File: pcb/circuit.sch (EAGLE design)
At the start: 136 parts, among them IC1 MCP73833-AMI/UN-ND, IC2 MCP3423, IC3 MCP1612-ADJI/MS, IC4 ATSAML22N18A, IC5 ATWINC1510-MR210PB1952-ND, IC6 RN4870, IC7 WE-TVS, J1 USB2-MICRO, J10 2.5MM-AUDIO-JACK-MONO, J11 2.5MM-AUDIO-JACK-MONO, J12 2.5MM-AUDIO-JACK-MONO, J13 2.5MM-AUDIO-JACK-MONO, J14 2.5MM-AUDIO-JACK-MONO, J2 S3B-XH-A, J3 2.5MM-AUDIO-JACK-MONO, J4 2.5MM-AUDIO-JACK-MONO, J5 2.5MM-AUDIO-JACK-MONO, J6 2.5MM-AUDIO-JACK-MONO, J7 2.5MM-AUDIO-JACK-MONO, J8 2.5MM-AUDIO-JACK-MONO, J9 2.5MM-AUDIO-JACK-MONO, Q1 32kHz, T1 PMOS, T10 NMOSSOT323, T11 NMOSSOT323, T12 NMOSSOT323, T13 NMOSSOT323, T2 NMOSSOT323, T3 NMOSSOT323, T4 NMOSSOT323, T5 NMOSSOT323, T6 NMOSSOT323, T7 NMOSSOT323, T8 NMOSSOT323, T9 NMOSSOT323, X1 B3S-1000

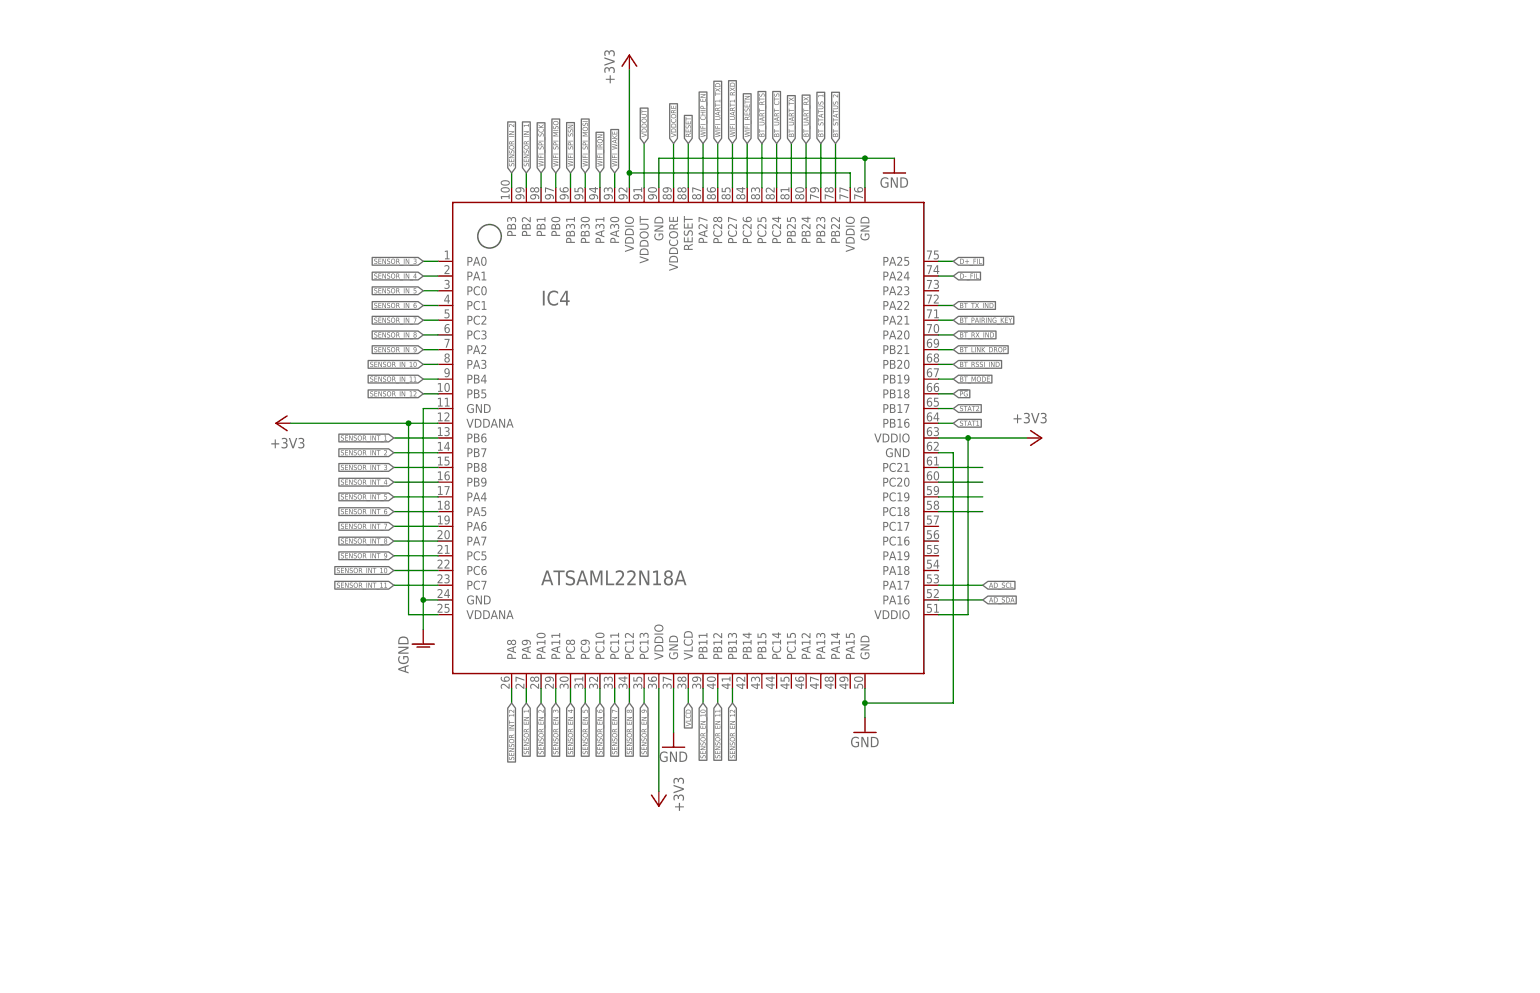
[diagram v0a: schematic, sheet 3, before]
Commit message: Schematic: - OLED added Datasheets: - SAML22 AppNotes added
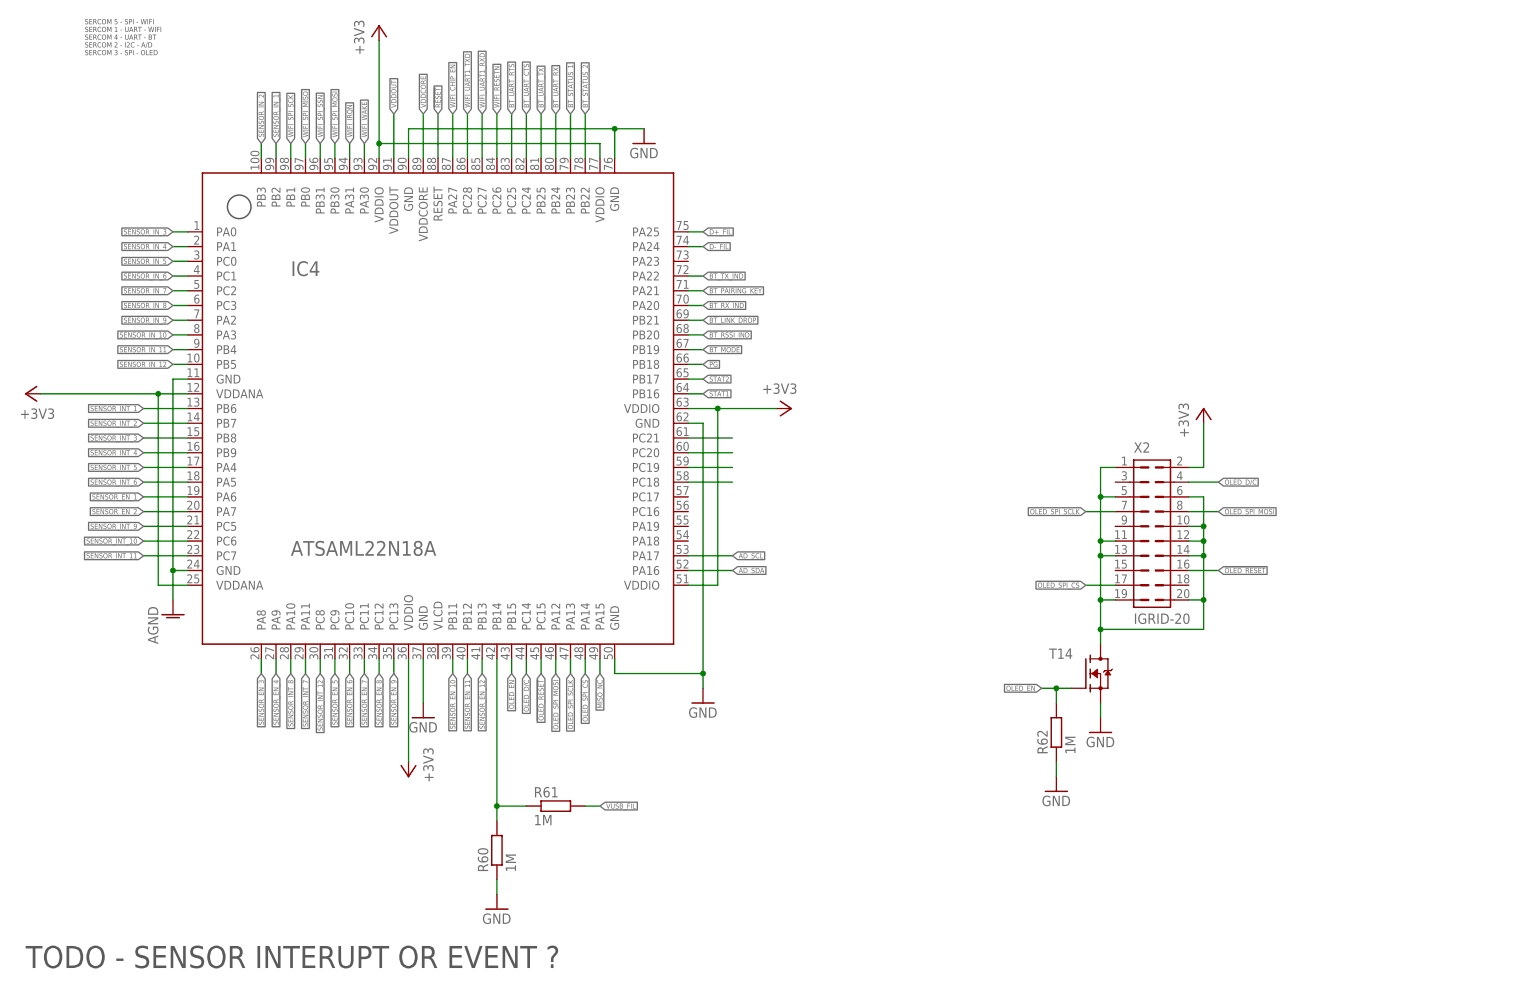
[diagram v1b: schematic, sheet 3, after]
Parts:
- added R60, R61, R62: 1M, rcl:R-EU_R0603
- added T14: NMOSSOT323, thermo:NMOSSOT323
- added X2: IGRID-20, thermo:IGRID-20
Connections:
- removed net VLCD: IC4.VLCD
- new net !OLED_RESET: IC4.PC15, X2.16
- new net !OLED_SPI_CS: IC4.PA14, X2.17
- new net MISO_NC: IC4.PA15
- new net N$31: IC4.PB14, R60.2, R61.1
- new net N$32: T14.D, X2.1, X2.10, X2.11, X2.12, X2.13, X2.14, X2.19, X2.20, X2.5, X2.6
- new net OLED_D/C: IC4.PC14, X2.4
- new net OLED_EN: IC4.PB15, R62.2, T14.G
- new net OLED_SPI_MOSI: IC4.PA12, X2.8
- new net OLED_SPI_SCLK: IC4.PA13, X2.7
- net +3V3: now also X2.2
- net GND: now also R60.1, R62.1, T14.S
- net SENSOR_EN_1: now also IC4.PA6; no longer IC4.PA9
- net SENSOR_EN_2: now also IC4.PA7; no longer IC4.PA10
- net SENSOR_EN_3: now also IC4.PA8; no longer IC4.PA11
- net SENSOR_EN_4: now also IC4.PA9; no longer IC4.PC8
- net SENSOR_INT_12: now also IC4.PC8; no longer IC4.PA8
- net SENSOR_INT_7: now also IC4.PA11; no longer IC4.PA6
- net SENSOR_INT_8: now also IC4.PA10; no longer IC4.PA7
- net VUSB_FIL: now also R61.2
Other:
- note added: "SERCOM 5 - SPI - WIFI SERCOM 1 - UART - WIFI SERCOM 4 - UART - BT SERCOM 2 - I2C - A/D SERCOM 3 - SPI - OLED"
- note added: "TODO - SENSOR INTERUPT OR EVENT ?"
- moved on the sheet: IC4

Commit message: Schematic
-added part numbers
-all devices are connected
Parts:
- removed J13, J14: 2.5MM-AUDIO-JACK-MONO, Thermo_Library:2.5MM-AUDIO-JACK-MONO
- removed R59: 4,7k, rcl:R-EU_R0603
- removed R60, R61, R62: 1M, rcl:R-EU_R0603
- removed T14: NMOSSOT323, thermo:NMOSSOT323
- added C27: 1nF, rcl:C-EUC0603
- added C33, C35, C36: 1µF, rcl:C-EUC0603
- added C34, C37: 100nF, rcl:C-EUC0603
- added IC8: ATSAML22N18A, Thermo_Library:ATSAML22N18A
- added JP1, JP2, JP4, JP7: (no value), jumper:JP4E
- added JP3: (no value), jumper:JP2E
- added JP5, JP6: (no value), jumper:JP1E
- added X3: MOLEX_1MM_FPC, thermo:MOLEX_1MM_FPC
- added X4: IGRID-20, thermo:IGRID-20
- C1, C2, C30, C5: OC_FARNELL 1735530 -> (none); OC_MOUSER (none) -> 81-GRM21BR61E106KA3L
- C10: value 100nF -> 1nF; device rcl:C-EUC0402 -> rcl:C-EUC0603; OC_FARNELL 2218856 -> (none); OC_MOUSER (none) -> 80-C0603C102K3R
- C11: value 100nF -> 4,7nF; device rcl:C-EUC0402 -> rcl:C-EUC0603; OC_FARNELL 2218856 -> (none); OC_MOUSER (none) -> 80-C0603C472K3R
- C12, C13, C14, C15, C19, C20, C3, C32, C6, C9: device rcl:C-EUC0402 -> rcl:C-EUC0603; OC_FARNELL 2218856 -> (none); OC_MOUSER (none) -> 581-06033C104KAT2A
- C16: value 1µF -> 100nF; device rcl:C-EUC0402 -> rcl:C-EUC0603; OC_FARNELL 2218856 -> (none); OC_MOUSER (none) -> 581-06033C104KAT2A
- C17, C18: value 22pF -> 10µF; device rcl:C-EUC0402 -> rcl:C-EUC0805; OC_FARNELL 2332500 -> (none); OC_MOUSER (none) -> 81-GRM21BR61E106KA3L
- C21, C22: value 10µF -> 100nF; device rcl:C-EUC0805 -> rcl:C-EUC0603; OC_FARNELL 1735530 -> (none); OC_MOUSER (none) -> 581-06033C104KAT2A
- C23: value 100nF -> 1µF; device rcl:C-EUC0402 -> rcl:C-EUC0603; OC_FARNELL 2218856 -> (none); OC_MOUSER (none) -> 810-CGA3E1X7R1E105AC
- C24: value 1µF -> 22pF; OC_FARNELL 2211179 -> (none); OC_MOUSER (none) -> 581-02013A220FAT2A
- C25: value 10µF -> 22pF; device rcl:C-EUC0805 -> rcl:C-EUC0603; OC_FARNELL 1735530 -> (none); OC_MOUSER (none) -> 581-02013A220FAT2A
- C26: value 10nF -> 10µF; device rcl:C-EUC0402 -> rcl:C-EUC0805; OC_FARNELL 1828887 -> (none); OC_MOUSER (none) -> 81-GRM21BR61E106KA3L
- C28: value 10nF -> 100nF; device rcl:C-EUC0402 -> rcl:C-EUC0603; OC_FARNELL 1828887 -> (none); OC_MOUSER (none) -> 581-06033C104KAT2A
- C29: value 4,7nF -> 10µF; device rcl:C-EUC0603 -> rcl:C-EUC0805; OC_FARNELL 1759098 -> (none); OC_MOUSER (none) -> 81-GRM21BR61E106KA3L
- C31: value 10µF -> 1nF; device rcl:C-EUC0805 -> rcl:C-EUC0603; OC_FARNELL 1735530 -> (none); OC_MOUSER (none) -> 80-C0603C102K3R
- C4, C7: device rcl:C-EUC0402 -> rcl:C-EUC0603; OC_FARNELL 1758911 -> (none); OC_MOUSER (none) -> 80-C0603C102K3R
- C8: value 100nF -> 10µF; device rcl:C-EUC0402 -> rcl:C-EUC0805; OC_FARNELL 2218856 -> (none); OC_MOUSER (none) -> 81-GRM21BR61E106KA3L
- D1: value BAT60AE6327HTSA1 -> Red; device Thermo_Library:BAT60AE6327HTSA1 -> Thermo_Library:LED-2012; OC_FARNELL 2432679 -> (none); OC_MOUSER (none) -> 630-HSMC-C170-T0000
- D2: value Red -> Green; OC_FARNELL 2750579 -> (none); OC_MOUSER (none) -> 630-HSMQ-C170-T0000
- D3: value Green -> Blue; OC_FARNELL 2750574 -> (none); OC_MOUSER (none) -> 630-HSMR-C170-R0000
- D4: value Blue -> BAT60AE6327HTSA1; device Thermo_Library:LED-2012 -> Thermo_Library:BAT60AE6327HTSA1; OC_FARNELL 2750580 -> (none); OC_MOUSER (none) -> 726-BAT60AE6327HTSA1
- IC1: OC_MOUSER (none) -> 579-MCP73833T-AMI/UN
- IC2: device Thermo_Library:MCP3423 -> thermo:MCP3423; OC_MOUSER (none) -> 579-MCP3423-E/UN
- IC3: device Thermo_Library:MCP1612-ADJI/MS -> thermo:MCP1612-ADJI/MS; OC_MOUSER (none) -> 579-MCP1612T-ADJI/MS
- IC4: value ATSAML22N18A -> WE-TVS; device Thermo_Library:ATSAML22N18A -> thermo:WE-TVS; OC_MOUSER (none) -> 710-824011
- IC5: OC_MOUSER (none) -> 556-1510MR210UB1140
- IC6: OC_MOUSER (none) -> 579-RN4870-V/RM118
- IC7: value WE-TVS -> MAX3378EEUD; device Thermo_Library:WE-TVS -> thermo:MAX3378EEUD; OC_MOUSER (none) -> 700-MAX3378EEUD
- J1: device Thermo_Library:USB2-MICRO -> thermo:USB2-MICRO; OC_MOUSER (none) -> 649-10104110-0001LF
- J10, J11, J3, J4, J5, J6, J7, J8, J9: OC_MOUSER (none) -> 490-MJ-2523-SMT-TR
- J12: value 2.5MM-AUDIO-JACK-MONO -> 22-05-7028-02; device Thermo_Library:2.5MM-AUDIO-JACK-MONO -> con-molex:22-05-7028-02; OC_MOUSER (none) -> 538-22-05-7028
- J2: value S3B-XH-A -> 2.5MM-AUDIO-JACK-MONO; device Thermo_Library:S3B-XH-A -> Thermo_Library:2.5MM-AUDIO-JACK-MONO; OC_FARNELL 2401852 -> (none); OC_MOUSER (none) -> 490-MJ-2523-SMT-TR
- L1: OC_FARNELL 2467201 -> (none); OC_MOUSER (none) -> 710-74437321033
- L2: value 10µH -> L-0603; device Thermo_Library:L-1210 -> Thermo_Library:L-0603; OC_FARNELL 1299975 -> (none); OC_MOUSER (none) -> 710-742792641
- L3: value L-0603 -> WE-CNSW; device Thermo_Library:L-0603 -> thermo:WE-CNSW; OC_FARNELL 1635705 -> (none); OC_MOUSER (none) -> 710-744232090
- L4: value WE-CNSW -> 10µH; device Thermo_Library:WE-CNSW -> Thermo_Library:L-1210; OC_MOUSER (none) -> 871-B82422H1103K
- L5: OC_FARNELL 1515716 -> (none); OC_MOUSER (none) -> 81-BLM18EG221SN1D
- R1: value 1M -> 270; OC_FARNELL 2447285 -> (none); OC_MOUSER (none) -> 652-CR0603FX-2700ELF
- R10: value 1.8M -> 2.2M; OC_FARNELL 9238875 -> (none); OC_MOUSER (none) -> 603-RC0603FR-072M2L
- R11: value 301k -> 1.8M; device rcl:R-EU_R0402 -> rcl:R-EU_R0603; OC_FARNELL 2059188 -> (none); OC_MOUSER (none) -> 603-RC0603FR-071M8L
- R12: value 10 -> 301k; device rcl:R-EU_R0402 -> rcl:R-EU_R0603; OC_FARNELL 2059188 -> (none); OC_MOUSER (none) -> 603-RC0603FR-07301KL
- R13: value 324k -> 1M; device rcl:R-EU_R0402 -> rcl:R-EU_R0603; OC_FARNELL 2302893 -> (none); OC_MOUSER (none) -> 603-RC0603FR-071ML
- R14: value 25k -> 10; device rcl:R-EU_R0805 -> rcl:R-EU_R0603; OC_DIGIKEY A124124CT-ND -> (none); OC_MOUSER (none) -> 603-RC0603FR-0710RL
- R15: value 200k -> 324k; device rcl:R-EU_R0402 -> rcl:R-EU_R0603; OC_FARNELL 2059185 -> (none); OC_MOUSER (none) -> 603-RC0603FR-07324KL
- R16: value 10k -> 25k; device rcl:R-EU_R0603 -> rcl:R-EU_R0805; OC_MOUSER (none) -> 279-CPF0805B25KE1
- R17: value 330 -> 200k; OC_MOUSER (none) -> 603-RC0603FR-07200KL
- R18, R21, R22, R23, R24, R25, R29: OC_FARNELL 2447743 -> (none); OC_MOUSER (none) -> 603-RC0603JR-070RL
- R19, R26: value 0 -> 1M; OC_FARNELL 2447743 -> (none); OC_MOUSER (none) -> 603-RC0603FR-071ML
- R2: value 270 -> 4,7k; device rcl:R-EU_R0402 -> rcl:R-EU_R0603; OC_FARNELL 2447144 -> (none); OC_MOUSER (none) -> 603-RC0603FR-074K7L
- R20: value 0 -> 100k; OC_FARNELL 2447743 -> (none); OC_MOUSER (none) -> 603-RT0603FRE13100KL
- R27: value 4.7k -> 0; device rcl:R-EU_R0402 -> rcl:R-EU_R0603; OC_FARNELL 9239316 -> (none); OC_MOUSER (none) -> 603-RC0603JR-070RL
- R28: value 1M -> 0; OC_MOUSER (none) -> 603-RC0603JR-070RL
- R3: value 270 -> 4,7k; device rcl:R-EU_R0402 -> rcl:R-EU_R0603; OC_FARNELL 2447144 -> (none)
- R30: value 1M -> 0; OC_FARNELL 2447285 -> (none); OC_MOUSER (none) -> 603-RC0603JR-070RL
- R31, R34, R48, R49, R50, R55, R56, R57: OC_FARNELL 2447285 -> (none); OC_MOUSER (none) -> 603-RC0603FR-071ML
- R32: value 1M -> 4,7k; OC_FARNELL 2447285 -> (none)
- R33: value 4,8k -> 0; OC_FARNELL 2447442 -> (none); OC_MOUSER (none) -> 603-RC0603JR-070RL
- R35, R51, R52, R53, R54: value 4,8k -> 1M; OC_FARNELL 2447442 -> (none); OC_MOUSER (none) -> 603-RC0603FR-071ML
- R36: value 4,8k -> 10k; OC_FARNELL 2447442 -> (none); OC_MOUSER (none) -> 603-RC0603FR-0710KL
- R37: value 1M -> 330; OC_FARNELL 2447285 -> (none); OC_MOUSER (none) -> 603-RC0603FR-07330RL
- R38, R43, R44, R45, R46: value 4,8k -> 4.7k 0.1%; OC_FARNELL 2447442 -> (none); OC_MOUSER (none) -> 279-CPF0603B4K7E1
- R39, R40, R41, R42, R47: value 1M -> 4.7k 0.1%; OC_FARNELL 2447285 -> (none); OC_MOUSER (none) -> 279-CPF0603B4K7E1
- R4: value 1.54k -> 100m; device rcl:R-EU_R0805 -> rcl:R-EU_R5025; OC_FARNELL 2670154 -> (none); OC_MOUSER (none) -> 652-CRM2010FXR100ELF
- R5: device rcl:R-EU_R0402 -> rcl:R-EU_R0603
- R58: value 4,7k -> 1M; OC_MOUSER (none) -> 603-RC0603FR-071ML
- R6: value 2k -> 1.54k; device rcl:R-EU_R0805 -> rcl:R-EU_R0603; OC_FARNELL 2447622 -> (none); OC_MOUSER (none) -> 660-RK73H1JTTD1541F
- R7: value 69.8k -> 270; device rcl:R-EU_R0805 -> rcl:R-EU_R0603; OC_FARNELL 1141002 -> 2447144
- R8: value 100m -> 2k; device rcl:R-EU_R5025 -> rcl:R-EU_R0603; OC_MOUSER (none) -> 652-CR0603-FX-2001LF
- R9: value 2.2M -> 69.8k; OC_FARNELL 2078930 -> (none); OC_MOUSER (none) -> 754-RR1220P-6982D-M
- SV1: value (none) -> JTAGEDU; OC_FARNELL 1392410 -> (none); OC_MOUSER (none) -> 538-70246-2004
- T1: device Thermo_Library:PMOS -> thermo:PMOS; OC_MOUSER (none) -> 781-SI2301CDS-T1-GE3
- T10, T11, T12, T13, T3, T4, T5, T6, T7, T8, T9: OC_FARNELL 2617470 -> (none); OC_MOUSER (none) -> 726-SP000917562
- T2: value NMOSSOT323 -> PMOS; device Thermo_Library:NMOSSOT323 -> thermo:PMOS; OC_FARNELL 2617470 -> (none); OC_MOUSER (none) -> 781-SI2301CDS-T1-GE3
- X1: value B3S-1000 -> LI-ION_BATHOL2; device Thermo_Library:B3S-1000 -> thermo:LI-ION_BATHOL2; OC_MOUSER (none) -> 534-1048
- X2: value IGRID-20 -> B3S-1000; device thermo:IGRID-20 -> Thermo_Library:B3S-1000; OC_MOUSER (none) -> 653-B3S-1000
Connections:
- removed net BAT_IN: IC2.CH1+, J2.VBAT+, R8.1, R9.1
- removed net N$10: C7.2, R14.2
- removed net N$11: C6.1, IC3.VCC, R12.1
- removed net N$18: R51.2, T13.D
- removed net N$25: IC4.PC21
- removed net N$26: IC4.PC20
- removed net N$27: IC4.PC19
- removed net N$28: IC4.PC18
- removed net N$31: IC4.PB14, R60.2, R61.1
- removed net N$9: IC3.COMP, R14.1
- removed net SENSOR_EN_10: IC4.PB11, R55.2
- removed net SENSOR_EN_11: IC4.PB12, R56.2
- removed net SENSOR_EN_12: IC4.PB13, R57.2
- removed net SENSOR_INT_10: IC4.PC6, J12.3
- removed net SENSOR_INT_11: IC4.PC7, J13.3
- removed net SENSOR_INT_12: IC4.PC8, J14.3
- removed net SENSOR_IN_10: IC4.PA3, J12.1, R53.1
- removed net SENSOR_IN_11: IC4.PB4, J13.1, R52.1
- removed net SENSOR_IN_12: IC4.PB5, J14.1, R51.1
- new net !PG!_TRANS: IC7.I/OVL1, IC8.PB18
- new net BUCK_RC_C: C10.2, R16.2
- new net BUCK_RC_R: IC3.COMP, R16.1
- new net BUCK_VCC: C9.1, IC3.VCC, R14.1
- new net EXT_PWM_0: IC8.PA19, J12-1.S
- new net EXT_PWM_1: IC8.PA18, J12-2.S
- new net RES0: IC8.PB13, JP3.1
- new net RES1: IC8.PB12, JP3.2
- new net RES2: IC8.PB11, JP3.3
- new net SENSOR_EN_0: IC8.PA4, R48.2, T3.G
- new net SENSOR_INT_0: IC8.PC8, J2.3
- new net SENSOR_IN_0: IC8.PB2, J2.1, R38.1
- new net SOF_NC: IC8.PA23
- new net STAT1_TRANS: IC7.I/OVL3, IC8.PB17
- new net STAT2_TRANS: IC7.I/OVL2, IC8.PB16
- new net UI_BUTTON_INT_0: IC8.PC21, X3.2
- new net UI_BUTTON_INT_1: IC8.PC20, X3.3
- new net UI_BUTTON_INT_2: IC8.PC19, X3.4
- new net UI_BUTTON_INT_3: IC8.PC18, X3.5
- new net USB_CON_INT_TRANS: IC7.I/OVL4, IC8.PB14
- new net VBAT_MEAS: C1.1, IC1.VBAT@1, IC1.VBAT@2, IC2.CH1-, R4.2, T1.D
- new net VIN: JP7.2, T2.D, X1.VBAT+
- net !OLED_RESET: now also IC8.PC15, X4.16; no longer IC4.PC15, X2.16
- net !OLED_SPI_CS: now also IC8.PA14, JP2.3, X4.17; no longer IC4.PA14, X2.17
- net !PG!: now also IC7.I/OVCC1, R7.2; no longer IC4.PB18, R5.2
- net !RESET!: now also C37.1, IC8.RESET, R36.1, R37.2; no longer C20.1, IC4.RESET, R16.1, R17.2
- net +3V3: now also C13.1, C14.1, C15.1, C16.1, C17.1, C2.1, C26.1, C27.1, C29.1, C34.1, C35.1, C6.1, C7.1, IC7.VL, IC8.VDDANA@1, IC8.VDDANA@2, IC8.VDDIO@1, IC8.VDDIO@2, IC8.VDDIO@3, IC8.VDDIO@4, IC8.VDDIO@5, J2.2, JP7.1, R12.2, R2.2, R26.2, R3.2, R32.2, R36.2, X3.1, X4.2; no longer C1.1, C10.1, C11.1, C21.1, C23.1, C25.1, C32.1, C8.1, IC4.VDDANA@1, IC4.VDDANA@2, IC4.VDDIO@1, IC4.VDDIO@2, IC4.VDDIO@3, IC4.VDDIO@4, IC4.VDDIO@5, J12.2, J13.2, J14.2, R11.2, R16.2, R27.2, R28.2, R58.2, R59.2, X2.2
- net AD_SCL: now also IC8.PA17, JP5.1, R2.1; no longer IC4.PA17, R58.1
- net AD_SDA: now also IC8.PA16, JP5.2, R3.1; no longer IC4.PA16, R59.1
- net AGND: now also C10.1, C11.2, C18.2, C19.2, C20.2, C21.2, IC8.GND@1, IC8.GND@2, R17.1, R18.2, R19.1; no longer C14.2, C15.2, C22.2, C29.2, C6.2, C7.1, IC4.GND@1, IC4.GND@2, R15.1, R32.1, T13.S, T2.S
- net BT_LINK_DROP: now also IC8.PB21; no longer IC4.PB21
- net BT_MODE: now also IC8.PB19, R31.1; no longer IC4.PB19, R28.1
- net BT_PAIRING_KEY: now also IC8.PA21; no longer IC4.PA21
- net BT_RSSI_IND: now also IC8.PB20; no longer IC4.PB20
- net BT_RX_IND: now also IC8.PA20; no longer IC4.PA20
- net BT_STATUS_1: now also IC8.PB23; no longer IC4.PB23
- net BT_STATUS_2: now also IC8.PB22; no longer IC4.PB22
- net BT_TX_IND: now also IC8.PA22; no longer IC4.PA22
- net BT_UART_CTS: now also IC8.PC24, JP4.2; no longer IC4.PC24
- net BT_UART_RTS: now also IC8.PC25, JP4.1; no longer IC4.PC25
- net BT_UART_RX: now also IC8.PB24, JP4.4; no longer IC4.PB24
- net BT_UART_TX: now also IC8.PB25, JP4.3; no longer IC4.PB25
- net D+: now also IC4.D+, L3.1; no longer IC7.D+, L4.1
- net D+_FIL: now also IC8.PA25, L3.2; no longer IC4.PA25, L4.2
- net D-: now also IC4.D-, L3.4; no longer IC7.D-, L4.4
- net D-_FIL: now also IC8.PA24, L3.3; no longer IC4.PA24, L4.3
- net FB: now also R15.1, R17.2; no longer R13.1, R15.2
- net GND: now also C14.2, C15.2, C22.2, C27.2, C29.2, C33.2, C34.2, C35.2, C36.2, C37.2, C6.2, C7.2, IC4.GND, IC8.GND@3, IC8.GND@4, IC8.GND@5, IC8.GND@6, IC8.GND@7, JP7.3, JP7.4, R11.1, R13.1, R18.1, R20.1, R35.1, R51.1, R52.1, R53.1, R54.1, R58.1, R8.1, R9.1, T13.S, X1.VBAT-, X2.P, X3.6; no longer C10.2, C11.2, C18.2, C19.2, C20.2, C21.2, IC4.GND@3, IC4.GND@4, IC4.GND@5, IC4.GND@6, IC4.GND@7, J2.VBAT-, R1.1, R10.1, R30.1, R37.1, R39.1, R40.1, R41.1, R42.1, R47.1, R6.1, R60.1, R62.1, R7.1, T14.S, X1.P
- net MISO_NC: now also IC8.PA15, JP2.4; no longer IC4.PA15
- net N$1: now also R11.2; no longer R9.2
- net N$12: now also D1.C, R1.1; no longer D2.C, R2.1
- net N$13: now also R12.1, R15.2; no longer R11.1, R13.2
- net N$14: now also D2.C, R5.1; no longer D3.C, R3.1
- net N$15: now also D3.C, R7.1; no longer D4.C, R5.1
- net N$16: now also R47.2, T12.D; no longer R53.2, T10.D
- net N$17: now also R20.2, T2.G; no longer R52.2, T12.D
- net N$2: now also R39.2, T4.D; no longer R46.2, T7.D
- net N$20: now also R40.2, T5.D; no longer R36.2, T2.D
- net N$21: now also R42.2, T7.D; no longer R35.2, T4.D
- net N$22: now also R44.2, T9.D; no longer R33.2, T5.D
- net N$23: now also C18.1, C19.1, C20.1; no longer C14.1, C22.1, C9.1
- net N$24: now also R21.2; no longer R29.2
- net N$29: now also R27.2; no longer R22.2
- net N$3: now also R41.2; no longer R45.2
- net N$30: now also R25.2; no longer R21.2
- net N$32: now also T13.D, X4.1, X4.10, X4.11, X4.12, X4.13, X4.14, X4.19, X4.20, X4.5, X4.6; no longer T14.D, X2.1, X2.10, X2.11, X2.12, X2.13, X2.14, X2.19, X2.20, X2.5, X2.6
- net N$37: now also C11.1, R19.2; no longer C29.1, R32.2
- net N$4: now also R43.2; no longer R44.2
- net N$45: now also R26.1; no longer R31.1
- net N$48: now also C30.1, C32.1; no longer C13.1, C26.1
- net N$5: now also R45.2, T10.D; no longer R43.2, T9.D
- net N$57: now also C33.1, R32.1; no longer C24.1, R27.1
- net N$6: now also R46.2; no longer R54.2
- net N$7: now also R37.1, X2.S; no longer R17.1, X1.S
- net NTC: now also R6.1, R9.2; no longer J2.NTC, R4.1, R7.2
- net OLED_D/C: now also IC8.PC14, X4.4; no longer IC4.PC14, X2.4
- net OLED_EN: now also IC8.PB15, R58.2, T13.G; no longer IC4.PB15, R62.2, T14.G
- net OLED_SPI_MOSI: now also IC8.PA12, JP2.1, X4.8; no longer IC4.PA12, X2.8
- net OLED_SPI_SCLK: now also IC8.PA13, JP2.2, X4.7; no longer IC4.PA13, X2.7
- net PROG: now also R8.2; no longer R6.2
- net RESET: now also C22.1; no longer C19.1
- net SENSOR_EN_1: now also IC8.PA5, R49.2, T5.G; no longer IC4.PA6, R37.2, T3.G
- net SENSOR_EN_2: now also IC8.PA6, R50.2, T7.G; no longer IC4.PA7, R39.2, T2.G
- net SENSOR_EN_3: now also IC8.PA7, R51.2, T9.G; no longer IC4.PA8, R40.2, T4.G
- net SENSOR_EN_4: now also IC8.PC5, R52.2, T11.G; no longer IC4.PA9, R41.2, T5.G
- net SENSOR_EN_5: now also IC8.PC6, R53.2, T4.G; no longer IC4.PC9, R42.2, T7.G
- net SENSOR_EN_6: now also IC8.PC7, R54.2; no longer IC4.PC10, R47.2
- net SENSOR_EN_7: now also IC8.PA9, R55.2; no longer IC4.PC11, R48.2
- net SENSOR_EN_8: now also IC8.PA10, R56.2, T10.G; no longer IC4.PC12, R49.2, T9.G
- net SENSOR_EN_9: now also IC8.PA11, R57.2, T12.G; no longer IC4.PC13, R50.2
- net SENSOR_INT_1: now also IC8.PC9, J4.3; no longer IC4.PB6, J3.3
- net SENSOR_INT_2: now also IC8.PC10, J6.3; no longer IC4.PB7, J4.3
- net SENSOR_INT_3: now also IC8.PC11, J8.3; no longer IC4.PB8, J5.3
- net SENSOR_INT_4: now also IC8.PC12, J10.3; no longer IC4.PB9, J6.3
- net SENSOR_INT_5: now also IC8.PC13, J3.3; no longer IC4.PA4, J7.3
- net SENSOR_INT_6: now also IC8.PB6, J5.3; no longer IC4.PA5, J8.3
- net SENSOR_INT_7: now also IC8.PB7, J7.3; no longer IC4.PA11, J9.3
- net SENSOR_INT_8: now also IC8.PB8, J9.3; no longer IC4.PA10, J10.3
- net SENSOR_INT_9: now also IC8.PB9; no longer IC4.PC5
- net SENSOR_IN_1: now also IC8.PB3, J4.1, R40.1; no longer IC4.PB2, J3.1, R38.1
- net SENSOR_IN_2: now also IC8.PC0, J6.1, R42.1; no longer IC4.PB3, J4.1, R36.1
- net SENSOR_IN_3: now also IC8.PC1, J8.1, R44.1; no longer IC4.PA0, J5.1, R35.1
- net SENSOR_IN_4: now also IC8.PC2, J10.1, R46.1; no longer IC4.PA1, J6.1, R33.1
- net SENSOR_IN_5: now also IC8.PC3, J3.1, R39.1; no longer IC4.PC0, J7.1, R46.1
- net SENSOR_IN_6: now also IC8.PA2, J5.1, R41.1; no longer IC4.PC1, J8.1, R45.1
- net SENSOR_IN_7: now also IC8.PA3, J7.1, R43.1; no longer IC4.PC2, J9.1, R44.1
- net SENSOR_IN_8: now also IC8.PB4, J9.1, R45.1; no longer IC4.PC3, J10.1, R43.1
- net SENSOR_IN_9: now also IC8.PB5, R47.1; no longer IC4.PA2, R54.1
- net STAT1: now also IC7.I/OVCC3, R1.2; no longer IC4.PB16, R2.2
- net STAT2: now also IC7.I/OVCC2, R5.2; no longer IC4.PB17, R3.2
- net SWDCLK: now also IC8.PA30
- net SWDIO: now also IC8.PA31
- net THERM: now also R6.2; no longer R4.2
- net V+: now also C8.1, D4.C, R14.2; no longer C2.1, D1.C, R12.2
- net VBAT: now also IC2.CH1+, R10.1, R4.1, T2.S; no longer C30.1, IC1.VBAT@1, IC1.VBAT@2, IC2.CH1-, R8.2, T1.D
- net VDDCORE: now also C21.1, C23.1, IC8.VDDCORE, L4.2; no longer C15.1, C16.1, IC4.VDDCORE, L2.2
- net VDDOUT: now also IC8.VDDOUT, L4.1; no longer IC4.VDDOUT, L2.1
- net VUSB: now also L2.2; no longer L3.2
- net VUSB_FIL: now also C36.1, IC4.VDD, IC7.!TS!, IC7.I/OVCC4, IC7.VCC, L2.1, R13.2; no longer IC7.VDD, L3.1, R1.2, R61.2
- net WIFI_CHIP_EN: now also IC8.PA27, R30.1; no longer IC4.PA27, R25.1
- net WIFI_CHIP_EN_D: now also R30.2, R35.2; no longer R25.2, R34.2
- net WIFI_IRQN: now also IC8.PC17, R22.1; no longer IC4.PA31, R18.1
- net WIFI_IRQN_D: now also R22.2; no longer R18.2
- net WIFI_RESETN: now also IC8.PC26, R33.1; no longer IC4.PC26, R26.1
- net WIFI_RESETN_D: now also R33.2, R34.2; no longer R26.2, R30.2
- net WIFI_SPI_MISO: now also IC8.PB0, JP1.2, R27.1; no longer IC4.PB0, R22.1
- net WIFI_SPI_MOSI: now also IC8.PB30, JP1.4, R24.1; no longer IC4.PB30, R20.1
- net WIFI_SPI_MOSI_D: now also R24.2; no longer R20.2
- net WIFI_SPI_SCK: now also IC8.PB1, JP1.1, R28.1; no longer IC4.PB1, R23.1
- net WIFI_SPI_SCK_D: now also R28.2; no longer R23.2
- net WIFI_SPI_SSN: now also IC8.PB31, JP1.3, R25.1; no longer IC4.PB31, R21.1
- net WIFI_UART1_RXD: now also IC8.PC27, JP6.2, R29.1; no longer IC4.PC27, R24.1
- net WIFI_UART1_RXD_D: now also R29.2; no longer R24.2
- net WIFI_UART1_TXD: now also IC8.PC28, JP6.1, R23.1; no longer IC4.PC28, R19.1
- net WIFI_UART1_TXD_D: now also R23.2; no longer R19.2
- net WIFI_WAKE: now also IC8.PC16, R21.1; no longer IC4.PA30, R29.1
- net XIN32: now also C24.1, IC8.PA0; no longer C17.1
- net XOUT32: now also C25.1, IC8.PA1; no longer C18.1
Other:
- note added: "Ground jumper"
- note added: "Polarity protection"
- note added: "SENSORINT[0..9] = EXINT[0..9] USB_Connected_INT = EXINT14 BUTTON_[0..3] = EXINT[10..13]"
- note added: "USB FILTER + ESD"
- note removed: "TODO - SENSOR INTERUPT OR EVENT ?"
